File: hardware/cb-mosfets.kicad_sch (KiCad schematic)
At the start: 29 parts, among them Q901 Q_NMOS_GDS, Q902 Q_NMOS_GDS

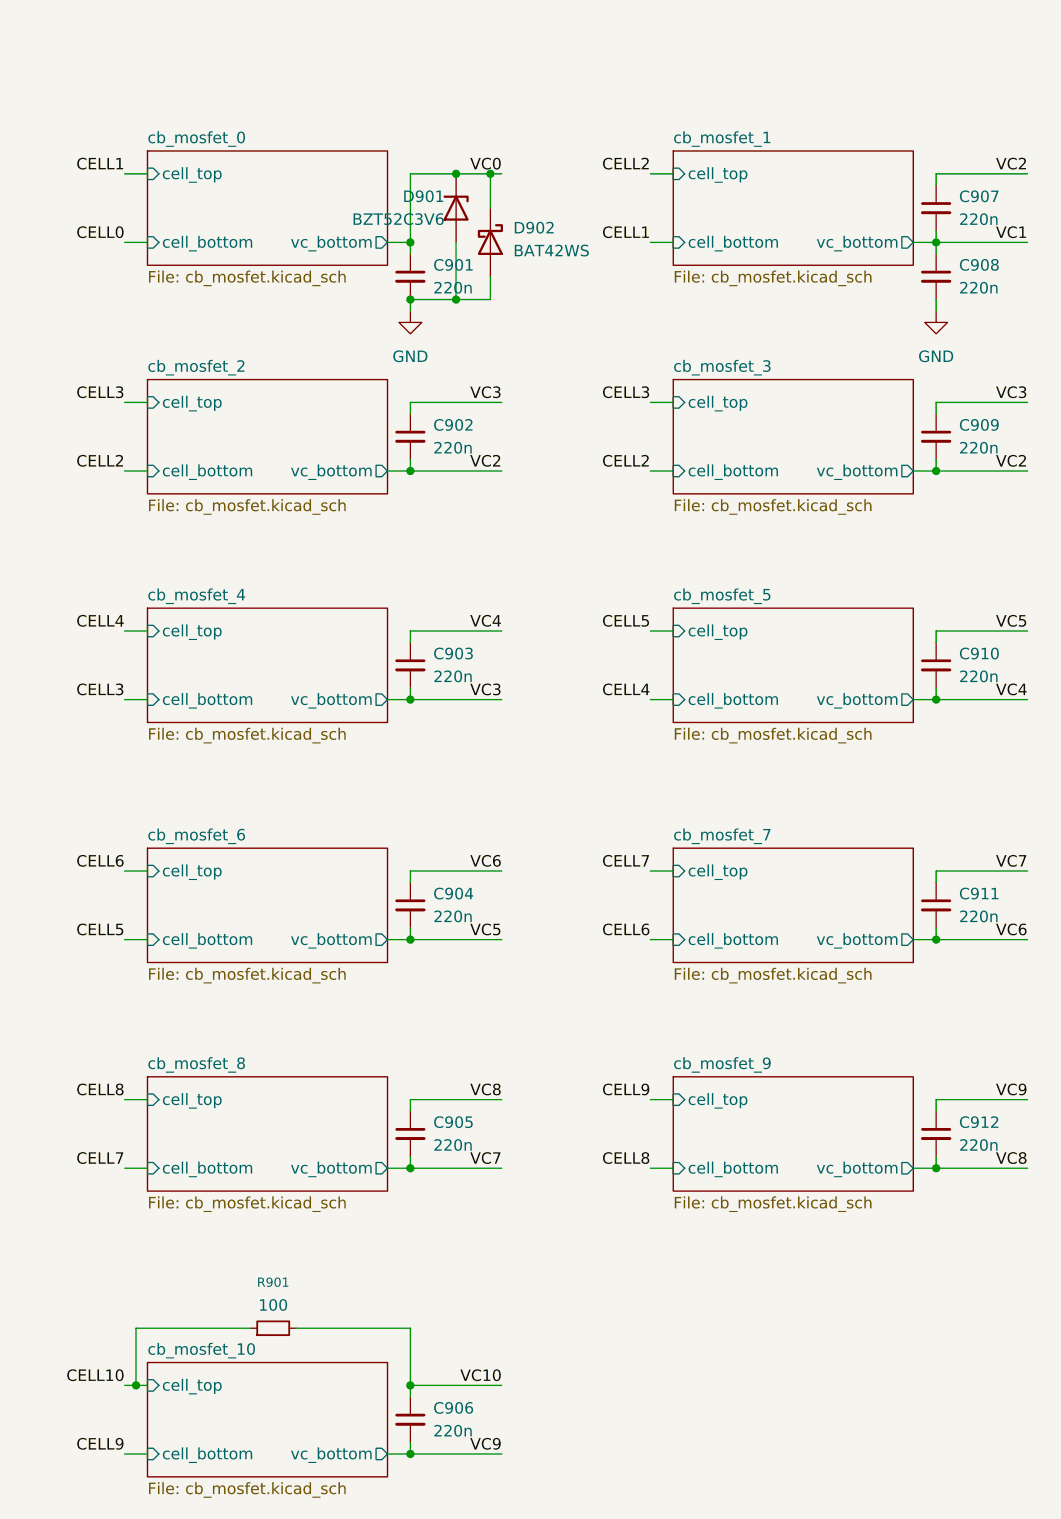
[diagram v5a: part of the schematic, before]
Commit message: fix MCU pin mapping and resolve ERC conflicts
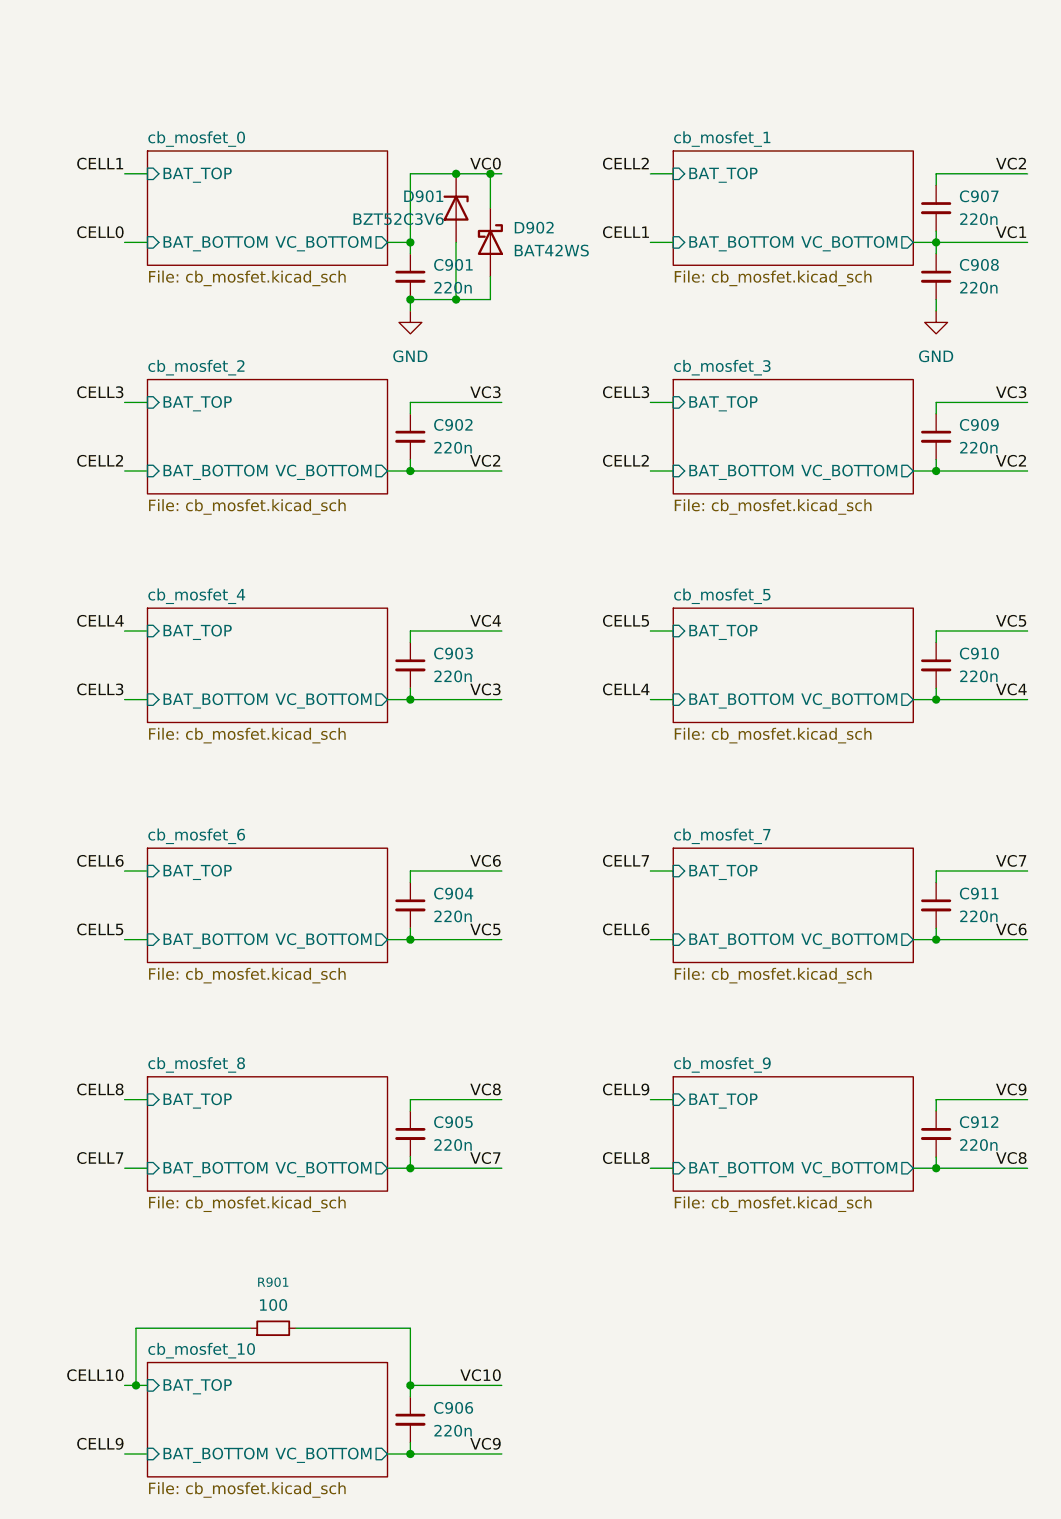
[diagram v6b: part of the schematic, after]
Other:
- sheet cb_mosfet_0 ports: added BAT_BOTTOM, BAT_TOP, VC_BOTTOM; removed cell_bottom, cell_top, vc_bottom
- sheet cb_mosfet_1 ports: added BAT_BOTTOM, BAT_TOP, VC_BOTTOM; removed cell_bottom, cell_top, vc_bottom
- sheet cb_mosfet_10 ports: added BAT_BOTTOM, BAT_TOP, VC_BOTTOM; removed cell_bottom, cell_top, vc_bottom
- sheet cb_mosfet_2 ports: added BAT_BOTTOM, BAT_TOP, VC_BOTTOM; removed cell_bottom, cell_top, vc_bottom
- sheet cb_mosfet_3 ports: added BAT_BOTTOM, BAT_TOP, VC_BOTTOM; removed cell_bottom, cell_top, vc_bottom
- sheet cb_mosfet_4 ports: added BAT_BOTTOM, BAT_TOP, VC_BOTTOM; removed cell_bottom, cell_top, vc_bottom
- sheet cb_mosfet_5 ports: added BAT_BOTTOM, BAT_TOP, VC_BOTTOM; removed cell_bottom, cell_top, vc_bottom
- sheet cb_mosfet_6 ports: added BAT_BOTTOM, BAT_TOP, VC_BOTTOM; removed cell_bottom, cell_top, vc_bottom
- sheet cb_mosfet_7 ports: added BAT_BOTTOM, BAT_TOP, VC_BOTTOM; removed cell_bottom, cell_top, vc_bottom
- sheet cb_mosfet_8 ports: added BAT_BOTTOM, BAT_TOP, VC_BOTTOM; removed cell_bottom, cell_top, vc_bottom
- sheet cb_mosfet_9 ports: added BAT_BOTTOM, BAT_TOP, VC_BOTTOM; removed cell_bottom, cell_top, vc_bottom

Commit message: first layout
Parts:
- D902: footprint (none) -> Diode_SMD:D_SOD-323F
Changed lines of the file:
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@@
 			)
 		)
-		(property "Footprint" ""
+		(property "Footprint" "Diode_SMD:D_SOD-323F"
 			(at 67.31 45.72 0)
 			(hide yes)

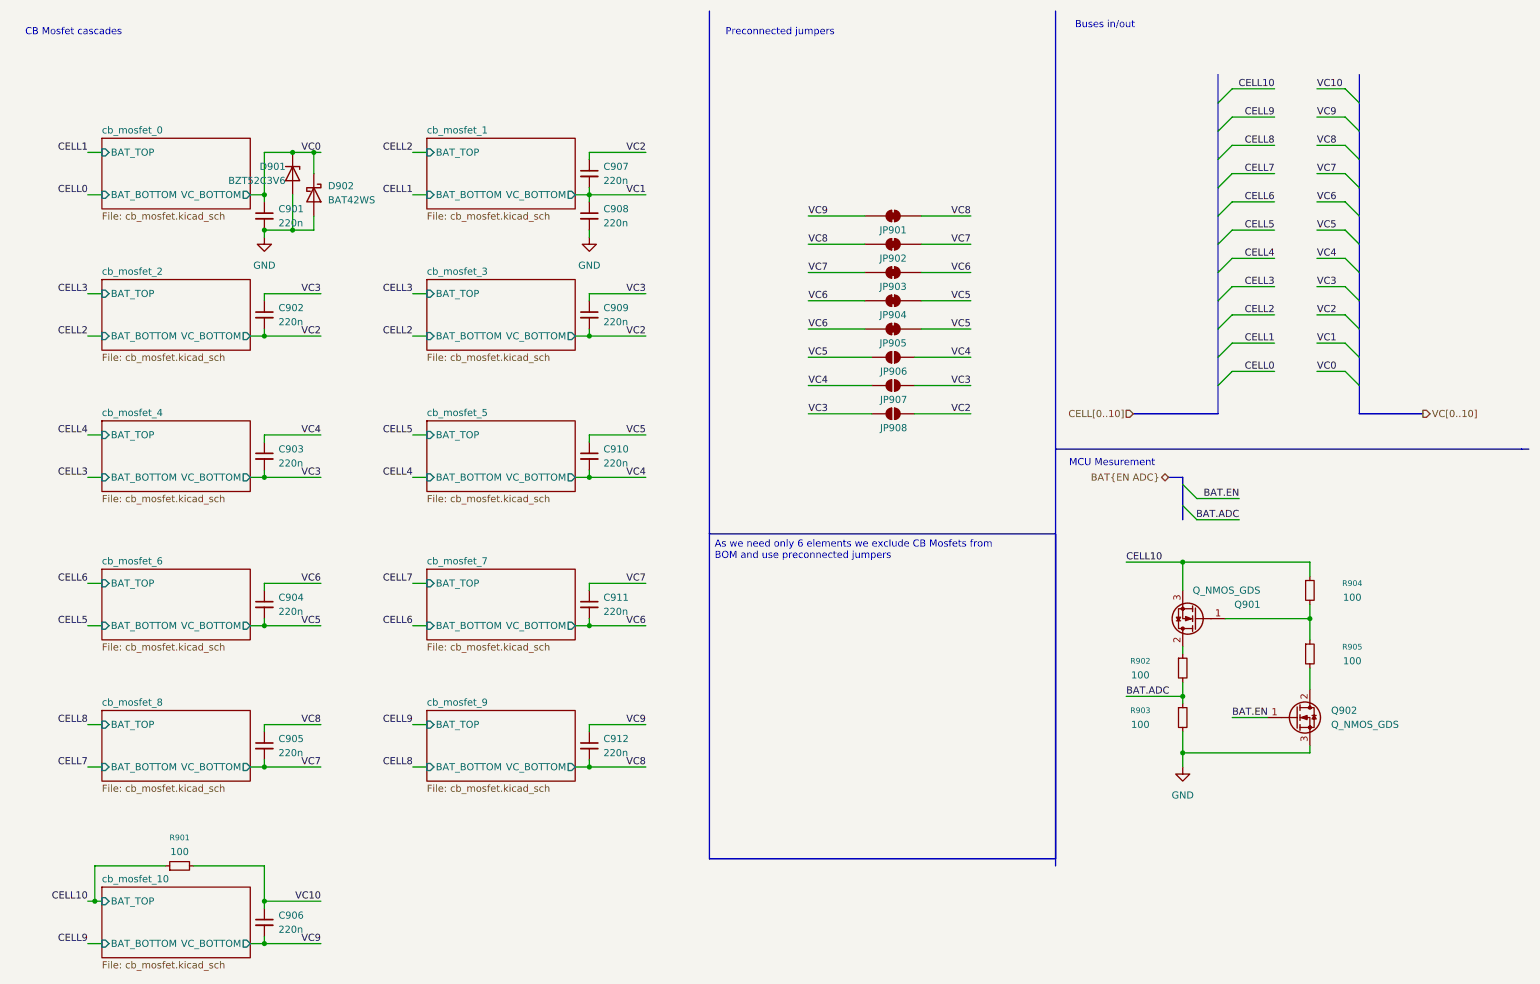
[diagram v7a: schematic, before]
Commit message: placed c mosfet
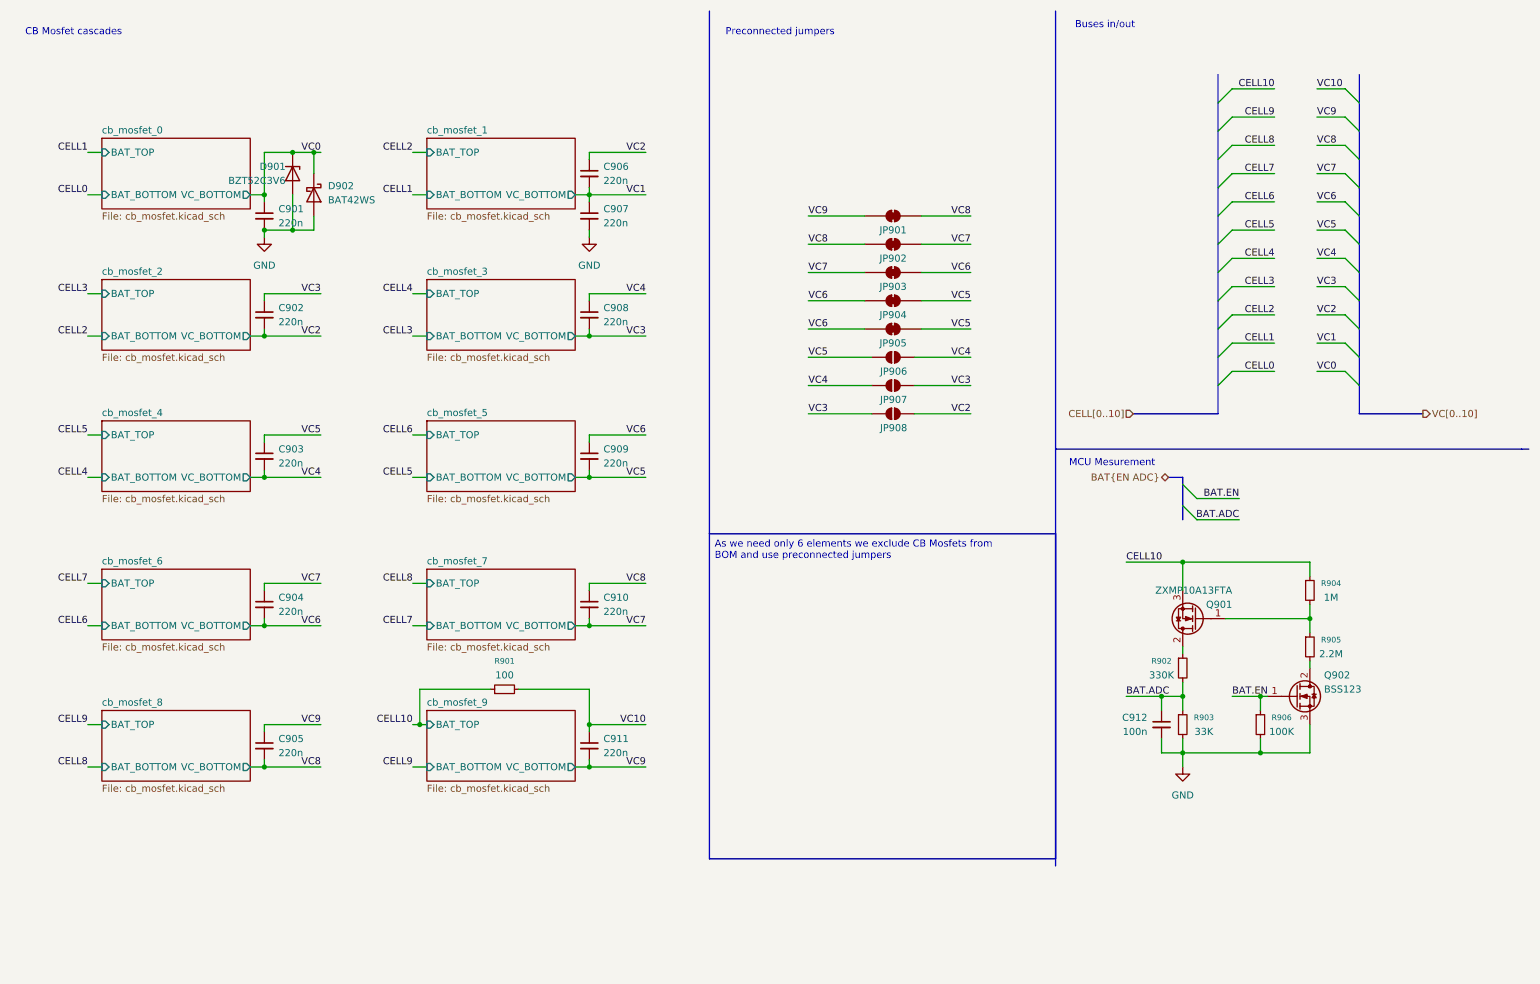
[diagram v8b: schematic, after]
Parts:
- removed C906: 220n, Capacitor_SMD:C_0805_2012Metric, symbol Device:C_Small
- added C912: 100n, Capacitor_SMD:C_0603_1608Metric, symbol Device:C_Small
- added R906: 100K, Resistor_SMD:R_0603_1608Metric, symbol Device:R_Small
- C901, C902, C903, C904, C905: footprint Capacitor_SMD:C_0805_2012Metric -> Capacitor_SMD:C_0603_1608Metric
- C906: renamed from C907; footprint Capacitor_SMD:C_0805_2012Metric -> Capacitor_SMD:C_0603_1608Metric
- C907: renamed from C908; footprint Capacitor_SMD:C_0805_2012Metric -> Capacitor_SMD:C_0603_1608Metric
- C908: renamed from C909; footprint Capacitor_SMD:C_0805_2012Metric -> Capacitor_SMD:C_0603_1608Metric
- C909: renamed from C910; footprint Capacitor_SMD:C_0805_2012Metric -> Capacitor_SMD:C_0603_1608Metric
- C910: renamed from C911; footprint Capacitor_SMD:C_0805_2012Metric -> Capacitor_SMD:C_0603_1608Metric
- C911: renamed from C912; footprint Capacitor_SMD:C_0805_2012Metric -> Capacitor_SMD:C_0603_1608Metric
- Q901: value Q_NMOS_GDS -> ZXMP10A13FTA; footprint (none) -> Package_TO_SOT_SMD:SOT-23
- Q902: value Q_NMOS_GDS -> BSS123; footprint (none) -> Package_TO_SOT_SMD:SOT-23
- R901: footprint Resistor_SMD:R_0805_2012Metric -> Resistor_SMD:R_0603_1608Metric
- R902: value 100 -> 330K; footprint Resistor_SMD:R_0805_2012Metric -> Resistor_SMD:R_0603_1608Metric
- R903: value 100 -> 33K; footprint Resistor_SMD:R_0805_2012Metric -> Resistor_SMD:R_0603_1608Metric
- R904: value 100 -> 1M; footprint Resistor_SMD:R_0805_2012Metric -> Resistor_SMD:R_0603_1608Metric
- R905: value 100 -> 2.2M; footprint Resistor_SMD:R_0805_2012Metric -> Resistor_SMD:R_0603_1608Metric
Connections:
- net BAT.ADC: now also C912.1
- net BAT.EN: now also R906.1
- net GND: now also C912.2, R906.2
- net VC10: now also C911.1
- net VC2: no longer C908.2
- net VC3: now also C908.2; no longer C903.2, C908.1
- net VC4: now also C903.2, C908.1; no longer C903.1, C909.2
- net VC5: now also C903.1, C909.2; no longer C904.2, C909.1
- net VC6: now also C904.2, C909.1; no longer C904.1, C910.2
- net VC7: now also C904.1, C910.2; no longer C905.2, C910.1
- net VC8: now also C905.2, C910.1; no longer C905.1, C911.2
- net VC9: now also C905.1, C911.2; no longer C911.1
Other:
- removed sheet cb_mosfet_10
- moved on the sheet: Q902, R903, R905
